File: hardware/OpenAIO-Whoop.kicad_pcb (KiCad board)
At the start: 6 copper layers, 30.3 x 30.3 mm, 266 parts, among them J1 U.FL, J10 M3, J13 M4, J16 TP0, J17 RP0, J18 5V, J19 GND, J2 +, J20 LED, J21 BZ+, J22 BZ-, J23 CAM, J24 5V, J25 GND, J26 VHD, J27 GND, J28 TX1, J29 RX1, J3 -, J31 USB, J32 CAM, J33 GND, J4 M1, J7 M2, Q26 AP1606, Q27 BC857BM, Q28 AP1606, Q29 AGM210MAP, Q30 AGM210MAP, Q31 AGM210MAP, Q32 AGM210MAP, Q33 AGM210MAP, Q34 AGM210MAP, Q35 AGM210MAP, Q36 AGM210MAP, Q37 AGM210MAP, Q38 AGM210MAP, Q39 AGM210MAP, Q40 AGM210MAP, SW1 SKUBAAE010, U1 INA186A3, U10 RP2354A, U11 BMI270, U12 TPS7A2018, U13 PY25Q128HA-DFH-IR, U14 SN74LVC1G3157, U15 TLV7031, U16 ESP32-PICO-V3, U18 SX1280, U19 RTC6705, U2 TPS61022, U20 SE5004L, U21 LP5912-3.3, U22 LP5907-2.85, U24 SGM40661, U3 TPS2116, U4 LP5912-3.3, U5 TPS22810, U6 EFM8BB51F16I, U7 EFM8BB51F16I, U8 EFM8BB51F16I, U9 EFM8BB51F16I, X1 12MHz 10pF, X3 52MHz TCXO, X4 8MHz 10pF

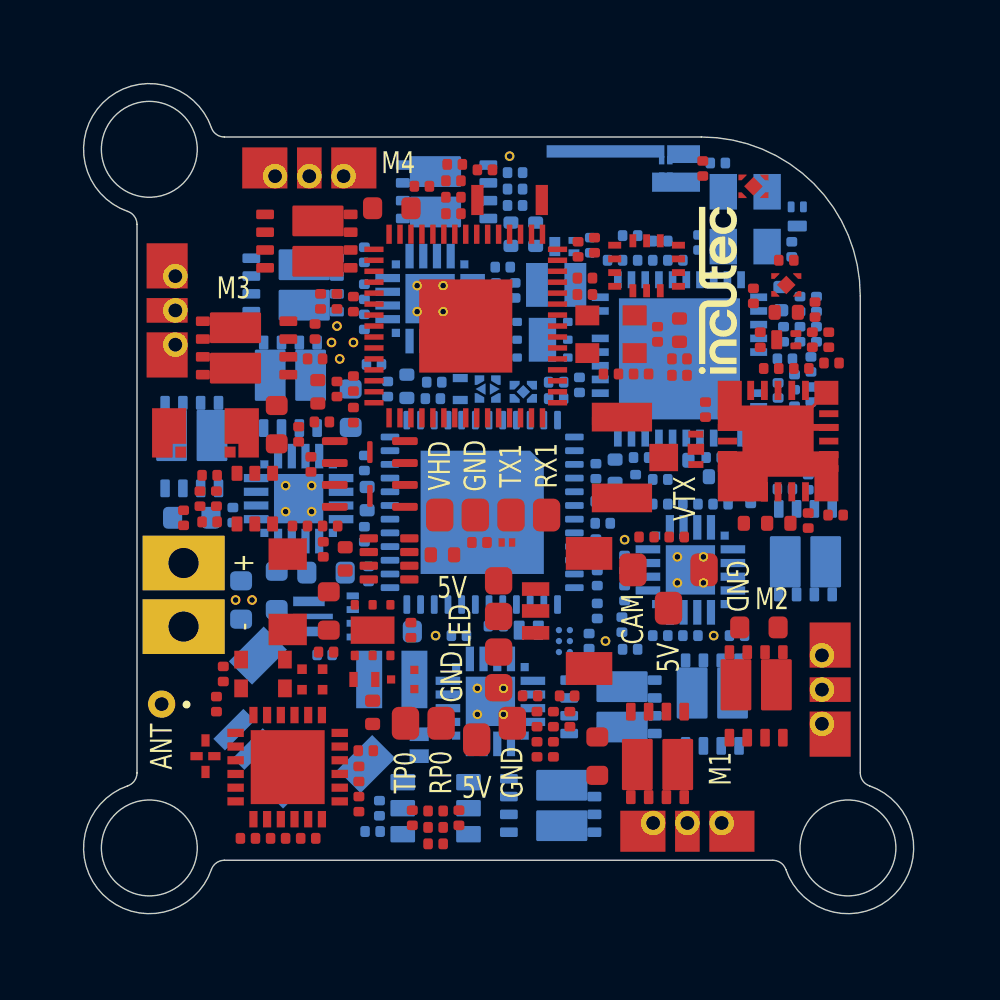
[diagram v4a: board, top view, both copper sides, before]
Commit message: hardware: floorplan v3 placed (272 footprints, Matrix-informed; DRC 0 errors, spacing 0; D72 mating zones + reserved via sites; D75 block outlines, function labels, RF paths; compaction: no empty patch > 1 mm2)
Co-Authored-By: Claude Opus 5.5 <noreply@anthropic.com>
Claude-Session: https://claude.ai/code/session_01RFaS5jnC9tnPam9GBgmGnG
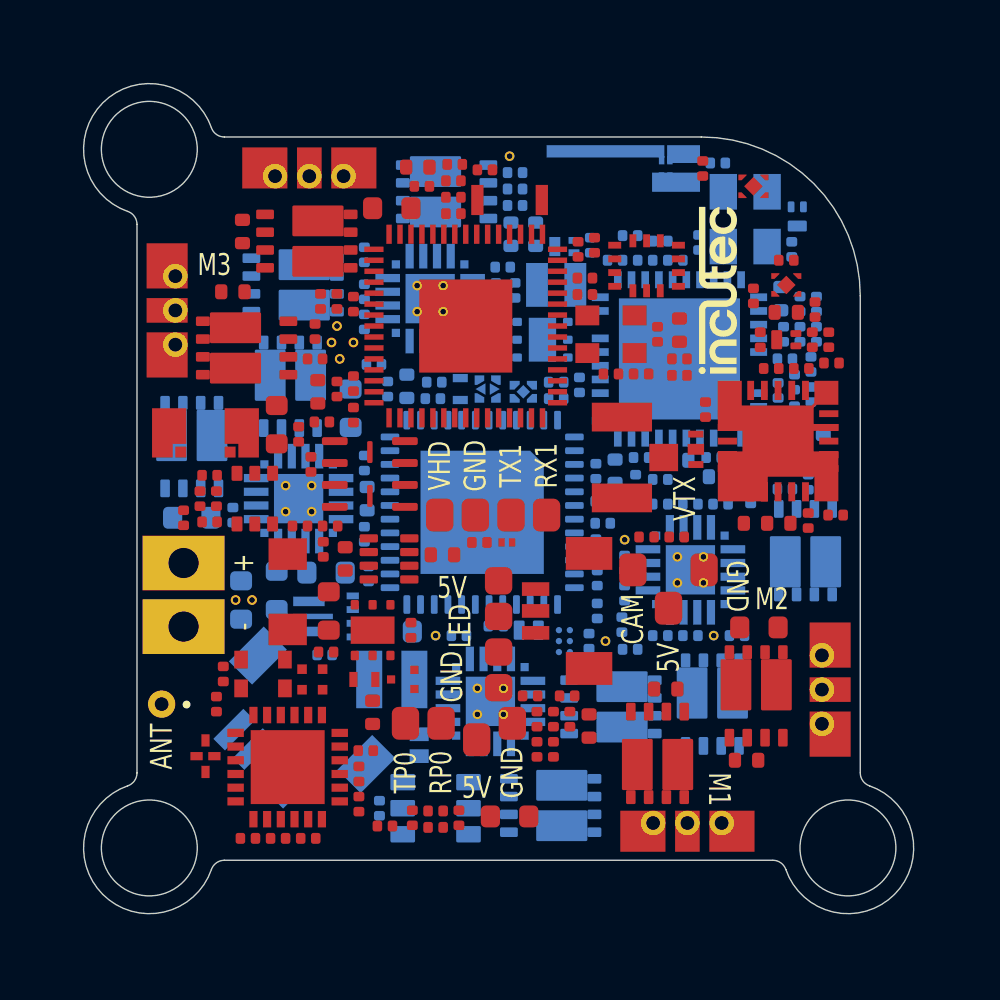
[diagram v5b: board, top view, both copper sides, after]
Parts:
- removed C17: 1uF, lib:C_0201_0603Metric_W
- removed C30: 2.2uF, lib:C_0402_1005Metric_W
- added C20: 10uF, lib:C_0402_1005Metric_W, F.Cu at (116.5, 121.5)
- added C21: 10uF, lib:C_0402_1005Metric_W, F.Cu at (119.3, 120.2)
- added C26: 10uF, lib:C_0402_1005Metric_W, B.Cu at (125.0, 111.3)
- added C27: 10uF, lib:C_0402_1005Metric_W, F.Cu at (122.2, 122.8)
- added C32: 10uF, lib:C_0402_1005Metric_W, B.Cu at (108.4, 113.2)
- added C33: 10uF, lib:C_0402_1005Metric_W, F.Cu at (103.5, 105.7)
- added C38: 10uF, lib:C_0402_1005Metric_W, F.Cu at (110.2, 101.1)
- added C39: 10uF, lib:C_0402_1005Metric_W, F.Cu at (103.8, 103.5)
- moved C23 3.88 mm to (113.6, 124.8), turned to 0 degrees
- moved R87 1.96 mm to (109.0, 125.2)
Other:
- board text removed: "M4"

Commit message: hardware: floorplan v3 review pass (RX RF corner blocker fixed; majors listed in FLOORPLAN.md Open)
Co-Authored-By: Claude Opus 5.5 <noreply@anthropic.com>
Claude-Session: https://claude.ai/code/session_01RFaS5jnC9tnPam9GBgmGnG
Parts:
- moved D4 9.68 mm to (115.3, 123.6)
- moved R7 5.25 mm to (102.9, 122.2), turned to 90 degrees
- moved C84 3.68 mm to (102.7, 123.2), turned to 0 degrees
- moved FL1 2.80 mm to (103.5, 120.0), turned to 180 degrees
- moved C85 2.32 mm to (104.6, 119.1), turned to 180 degrees
- moved X3 1.70 mm to (106.3, 119.7)

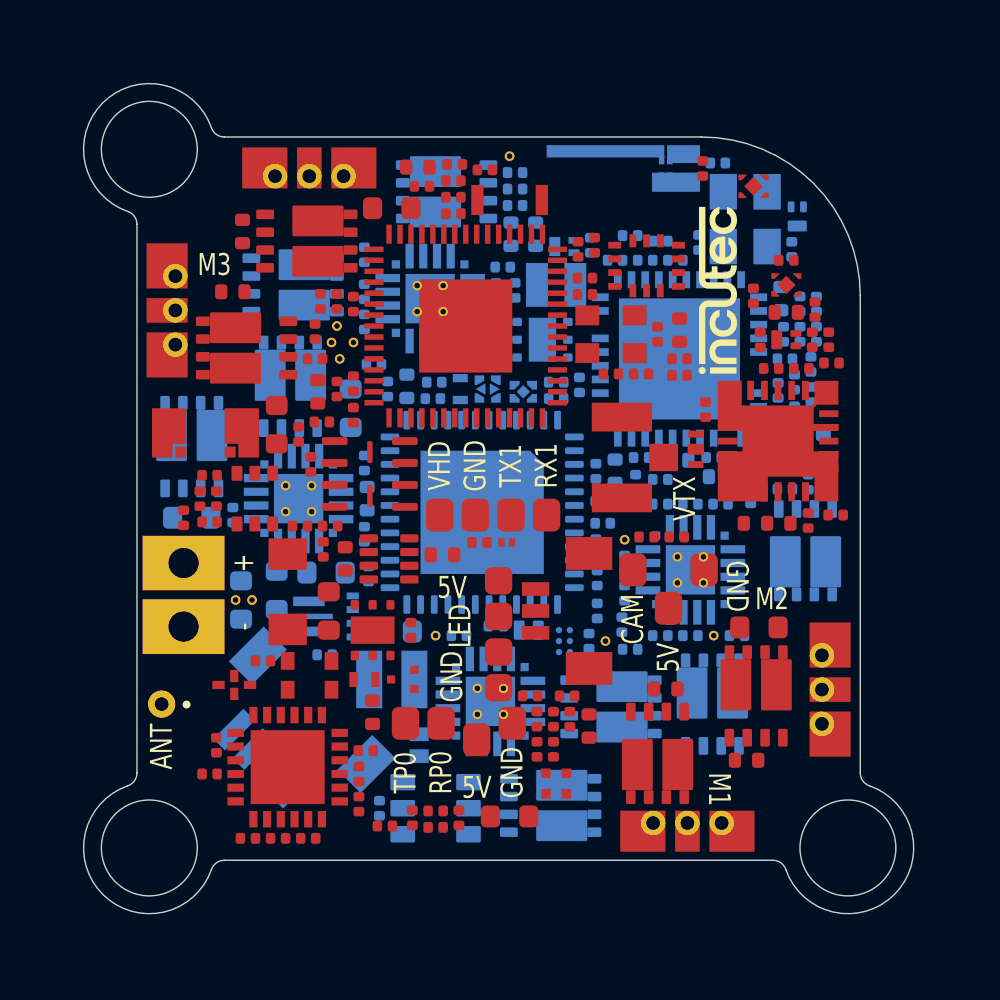
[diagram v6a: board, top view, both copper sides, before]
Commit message: hardware: schematic synced to the board (271 parts, 263 nets, parity 0 errors; SPI net patterns fixed in the DRU; X1 3225 placed)
Co-Authored-By: Claude Opus 5.5 <noreply@anthropic.com>
Claude-Session: https://claude.ai/code/session_01RFaS5jnC9tnPam9GBgmGnG
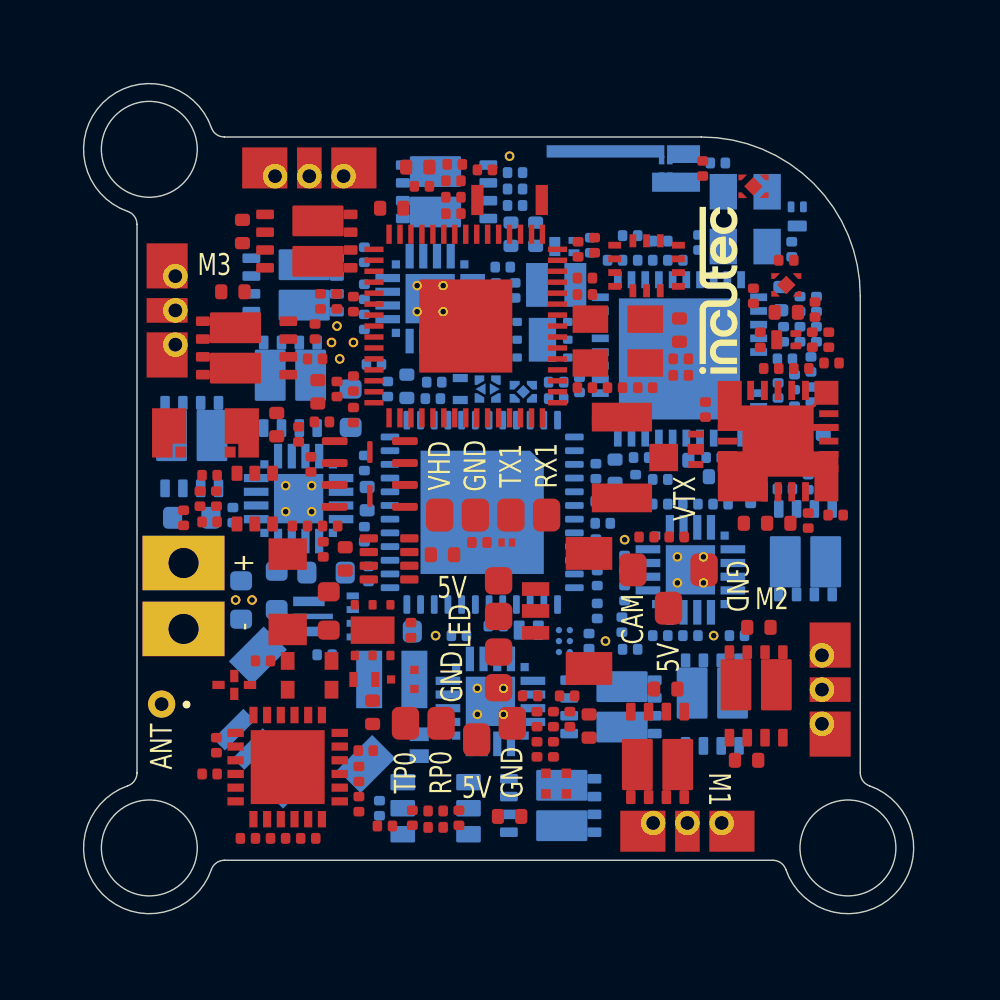
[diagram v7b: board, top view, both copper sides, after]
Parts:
- AE1: value ANT 2.4G wire -> ANT
- C124, C125: value 100nF -> 1uF
- C23, C29, C35, C41: value 22uF -> 10uF; footprint lib:C_0603_1608Metric_W -> lib:C_0402_1005Metric_W
- FL1: value LPF 2.4G -> 2450FM07D0034T; footprint lib:FILTER-SMD_4P-L1.0-W0.5-L_DEA102700LT-XXX_W -> lib:FILTER-SMD_4P-L1.0-W0.5-L_W
- J21: value BZ+ -> 5V
- R10: value 49.9k -> 18k
- R11: value 4.7k -> 2.4k
- R4: value 909k -> 47k
- R41: value 30R -> 27R
- R5: value 120k -> 6.2k
- R71, R72: value 18k -> 1k
- R73: value 10k -> 10R
- R84: value 10k -> 1k
- R9: value 80.6k -> 33k
- U18: value SX1280 -> SX1281
- X1: value 12MHz 10pF -> 12MHz; footprint lib:CRYSTAL-SMD_4P-L2.5-W2.0-BL-A_Dense -> lib:CRYSTAL-SMD_4P-L3.2-W2.5-BL_Dense
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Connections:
- AE1 pad 1: (no net) -> /RX/RF_RX_ANT
- AE2 pad 1: /FLOORPLAN/AE2_1_4 -> /RX/RF_WIFI_ANT
- AE2 pad 2: /FLOORPLAN/AE2_2 -> GND
- AE2 pad 3: /FLOORPLAN/AE2_3 -> GND
- AE2 pad 4: /FLOORPLAN/AE2_1_4 -> /RX/RF_WIFI_ANT
- C1 pad 1: (no net) -> +BATT_IN
- C1 pad 2: (no net) -> GND
- C10 pad 1: (no net) -> +5V_BST
- C10 pad 2: (no net) -> GND
- C100 pad 1: (no net) -> +3V3_VTX
- C100 pad 2: (no net) -> GND
- C101 pad 1: (no net) -> +3V3_VTX
- C101 pad 2: (no net) -> GND
- C102 pad 1: (no net) -> +3V3_VTX
- C102 pad 2: (no net) -> GND
- C103 pad 1: (no net) -> +3V3_VTX
- C103 pad 2: (no net) -> GND
- C104 pad 1: (no net) -> /VIDEO_OUT
- C104 pad 2: (no net) -> /VTX/VT_MOD_N1
- C105 pad 1: (no net) -> /VTX/VT_MOD_N1
- C105 pad 2: (no net) -> /VTX/VT_MOD_N2
- C106 pad 1: (no net) -> /VTX/RTC_VT
- C106 pad 2: (no net) -> GND
- C107 pad 1: (no net) -> /VTX/RTC_LF
- C107 pad 2: (no net) -> GND
- C108 pad 1: (no net) -> +3V3_VTX
- C108 pad 2: (no net) -> GND
- C109 pad 1: (no net) -> /VTX/PAOUT1_SUP
- C109 pad 2: (no net) -> GND
- C11 pad 1: (no net) -> +5V_BST
- C11 pad 2: (no net) -> GND
- C110 pad 1: (no net) -> /VTX/RF_PAOUT1
- C110 pad 2: (no net) -> /VTX/RF_PA_IN
- C111 pad 1: (no net) -> /VTX/PA_VCC
- C111 pad 2: (no net) -> GND
- C112 pad 1: (no net) -> /VTX/PA_VCC
- C112 pad 2: (no net) -> GND
- C113 pad 1: (no net) -> /VTX/PA_VCC
- C113 pad 2: (no net) -> GND
- C114 pad 1: (no net) -> /VTX/PA_VCC
- C114 pad 2: (no net) -> GND
- C115 pad 1: (no net) -> /VTX/PA_VCC
- C115 pad 2: (no net) -> GND
- C116 pad 1: (no net) -> /VTX/PA_VCC
- C116 pad 2: (no net) -> GND
- C117 pad 1: (no net) -> /PA_DET
- C117 pad 2: (no net) -> GND
- C118 pad 1: (no net) -> /VTX/PA_VCC
- C118 pad 2: (no net) -> GND
- C12 pad 1: (no net) -> +5V
- C12 pad 2: (no net) -> GND
- C121 pad 1: (no net) -> +3V3_VTX
- C121 pad 2: (no net) -> GND
- C122 pad 1: (no net) -> +3V3_VTX
- C122 pad 2: (no net) -> GND
- C123 pad 1: (no net) -> /VTX/PA_VREF
- C123 pad 2: (no net) -> GND
- C124 pad 1: (no net) -> /VTX/PA_RC1
- C124 pad 2: (no net) -> GND
- C125 pad 1: (no net) -> /VTX/Q27_B
- C125 pad 2: (no net) -> GND
- C128 pad 1: (no net) -> +5V_USB
- C128 pad 2: (no net) -> GND
- C129 pad 1: (no net) -> /POWER/U5_EN
- C129 pad 2: (no net) -> GND
- C13 pad 1: (no net) -> +5V
- C13 pad 2: (no net) -> GND
- C131 pad 1: (no net) -> /VBUS
- C131 pad 2: (no net) -> GND
- C132 pad 1: (no net) -> /RX/RF_WIFI_ANT
- C132 pad 2: (no net) -> GND
- C133 pad 1: (no net) -> /RX/RF_WIFI
- C133 pad 2: (no net) -> GND
- C134 pad 1: (no net) -> +1V1
- C134 pad 2: (no net) -> GND
- C14 pad 1: (no net) -> +3V3
- C14 pad 2: (no net) -> GND
- C15 pad 1: (no net) -> +5V_CAM
- C15 pad 2: (no net) -> GND
- C16 pad 1: (no net) -> /POWER/U5_CT
- C16 pad 2: (no net) -> GND
- C19 pad 1: (no net) -> +BATT
- C19 pad 2: (no net) -> GND
- C2 pad 1: (no net) -> +BATT_IN
- C2 pad 2: (no net) -> GND
- C20 pad 1: (no net) -> +BATT
- C20 pad 2: (no net) -> GND
- C21 pad 1: (no net) -> +BATT
- C21 pad 2: (no net) -> GND
- C23 pad 1: (no net) -> +BATT
- C23 pad 2: (no net) -> GND
- C25 pad 1: (no net) -> +BATT
- C25 pad 2: (no net) -> GND
- C26 pad 1: (no net) -> +BATT
- C26 pad 2: (no net) -> GND
- C27 pad 1: (no net) -> +BATT
- C27 pad 2: (no net) -> GND
- C29 pad 1: (no net) -> +BATT
- C29 pad 2: (no net) -> GND
- C31 pad 1: (no net) -> +BATT
- C31 pad 2: (no net) -> GND
- C32 pad 1: (no net) -> +BATT
- C32 pad 2: (no net) -> GND
- C33 pad 1: (no net) -> +BATT
- C33 pad 2: (no net) -> GND
- C35 pad 1: (no net) -> +BATT
- C35 pad 2: (no net) -> GND
- C37 pad 1: (no net) -> +BATT
- C37 pad 2: (no net) -> GND
- C38 pad 1: (no net) -> +BATT
- C38 pad 2: (no net) -> GND
- C39 pad 1: (no net) -> +BATT
- C39 pad 2: (no net) -> GND
- C41 pad 1: (no net) -> +BATT
- C41 pad 2: (no net) -> GND
- C42 pad 1: (no net) -> /RP2350A/XIN
- C42 pad 2: (no net) -> GND
- C43 pad 1: (no net) -> /RP2350A/XOUT_X
- C43 pad 2: (no net) -> GND
- C44 pad 1: (no net) -> +3V3
- C44 pad 2: (no net) -> GND
- C45 pad 1: (no net) -> +3V3
- C45 pad 2: (no net) -> GND
- C46 pad 1: (no net) -> +3V3
- C46 pad 2: (no net) -> GND
- C47 pad 1: (no net) -> +3V3
- C47 pad 2: (no net) -> GND
- C48 pad 1: (no net) -> +3V3
- C48 pad 2: (no net) -> GND
- C49 pad 1: (no net) -> +3V3
- C49 pad 2: (no net) -> GND
- C5 pad 1: (no net) -> /POWER/SHUNT_SENSE_N_RC
- C5 pad 2: (no net) -> /POWER/SHUNT_SENSE_P_RC
- C50 pad 1: (no net) -> +1V1
- C50 pad 2: (no net) -> GND
- C51 pad 1: (no net) -> +1V1
- C51 pad 2: (no net) -> GND
- C52 pad 1: (no net) -> +1V1
- C52 pad 2: (no net) -> GND
- C54 pad 1: (no net) -> +3V3
- C54 pad 2: (no net) -> GND
- C56 pad 1: (no net) -> +1V1
- C56 pad 2: (no net) -> GND
- C57 pad 1: (no net) -> /RP2350A/VREG_AVDD
- C57 pad 2: (no net) -> GND
- C58 pad 1: (no net) -> +3V3
- C58 pad 2: (no net) -> GND
- C59 pad 1: (no net) -> GND
- C59 pad 2: (no net) -> /RP2350A/ADC_VBAT
- C6 pad 1: (no net) -> +3V3
- C6 pad 2: (no net) -> GND
- C60 pad 1: (no net) -> /RP2350A/ADC_CURR
- C60 pad 2: (no net) -> GND
- C61 pad 1: (no net) -> +3V3
- C61 pad 2: (no net) -> GND
- C62 pad 1: (no net) -> +1V8
- C62 pad 2: (no net) -> GND
- C65 pad 1: (no net) -> +3V3
- C65 pad 2: (no net) -> GND
- C66 pad 1: (no net) -> /VIDEO_IN
- C66 pad 2: (no net) -> GND
- C67 pad 1: (no net) -> /OSD/VID_FILT
- C67 pad 2: (no net) -> GND
- C68 pad 1: (no net) -> /OSD/VID_FILT
- C68 pad 2: (no net) -> /OSD/VID_DC
- C7 pad 1: (no net) -> +BATT
- C7 pad 2: (no net) -> GND
- C70 pad 1: (no net) -> +3V3
- C70 pad 2: (no net) -> GND
- C73 pad 1: (no net) -> /RX/RX_EN
- C73 pad 2: (no net) -> GND
- C76 pad 1: (no net) -> +3V3
- C76 pad 2: (no net) -> GND
- C8 pad 1: (no net) -> +5V_BST
- C8 pad 2: (no net) -> GND
- C82 pad 1: (no net) -> +3V3
- C82 pad 2: (no net) -> GND
- C83 pad 1: (no net) -> +3V3
- C83 pad 2: (no net) -> GND
- C84 pad 1: (no net) -> /RX/TCXO_OUT
- C84 pad 2: (no net) -> /RX/XTA
- C85 pad 1: (no net) -> +3V3
- C85 pad 2: (no net) -> GND
- C86 pad 1: (no net) -> /RX/VR_PA
- C86 pad 2: (no net) -> GND
- C87 pad 1: (no net) -> GND
- C87 pad 2: (no net) -> /RX/VREG_RADIO
- C88 pad 1: (no net) -> GND
- C88 pad 2: (no net) -> /RX/VREG_RADIO
- C89 pad 1: (no net) -> +3V3
- C89 pad 2: (no net) -> GND
- C9 pad 1: (no net) -> +5V_BST
- C9 pad 2: (no net) -> GND
- C91 pad 1: (no net) -> +3V3
- C91 pad 2: (no net) -> GND
- C92 pad 1: (no net) -> +3V3
- C92 pad 2: (no net) -> GND
- C94 pad 1: (no net) -> /VTX/U19_XTAL1
- C94 pad 2: (no net) -> GND
- C95 pad 1: (no net) -> /VTX/U19_XTAL2
- C95 pad 2: (no net) -> GND
- C96 pad 1: (no net) -> /VTX/U19_REG1D8
- C96 pad 2: (no net) -> GND
- C98 pad 1: (no net) -> +3V3_VTX
- C98 pad 2: (no net) -> GND
- D1 pad 1: (no net) -> +BATT_IN
- D1 pad 2: (no net) -> GND
- D2 pad 1: (no net) -> /HD_EN
- D2 pad 2: (no net) -> /POWER/U5_EN
- D3 pad 1: (no net) -> /OSD/VID_DC
- D3 pad 2: (no net) -> GND
- D4 pad 1: (no net) -> unconnected-(D4-DOUT-Pad1)
- D4 pad 2: (no net) -> +3V3
- D4 pad 3: (no net) -> GND
- D4 pad 4: (no net) -> /RX/RX_LED
- D5 pad 1: (no net) -> /LED/D5_K
- D5 pad 2: (no net) -> +3V3
- D6 pad 1: (no net) -> /LED/D6_K
- D6 pad 2: (no net) -> +3V3
- D7 pad 1: (no net) -> /USB_D_P
- D7 pad 2: (no net) -> /USB_D_N
- D7 pad 3: (no net) -> GND
- D8 pad 1: (no net) -> /FC_BOOT
- D8 pad 2: (no net) -> /RX/RX_BOOT
- D8 pad 3: (no net) -> /RX/BOOT_SW
- FB1 pad 1: (no net) -> +5V
- FB1 pad 2: (no net) -> +5V_CAM
- FL1 pad 1: (no net) -> /RX/RF_RFIO
- FL1 pad 2: (no net) -> GND
- FL1 pad 3: (no net) -> /RX/RF_RX_ANT
- FL1 pad 4: (no net) -> GND
- FL2 pad 1: (no net) -> /VTX/RF_PA_OUT
- FL2 pad 2: (no net) -> GND
- FL2 pad 3: (no net) -> /VTX/RF_UFL
- J1 pad 1: (no net) -> /VTX/RF_UFL
- J1 pad 2: (no net) -> GND
- J1 pad 3: (no net) -> GND
- J10 pad 1: /FLOORPLAN/J10_1 -> /ESC3/PHASE_C
- J10 pad 2: /FLOORPLAN/J10_2 -> /ESC3/PHASE_B
- J10 pad 3: /FLOORPLAN/J10_3 -> /ESC3/PHASE_A
- J13 pad 1: /FLOORPLAN/J13_1 -> /ESC4/PHASE_C
- J13 pad 2: /FLOORPLAN/J13_2 -> /ESC4/PHASE_B
- J13 pad 3: /FLOORPLAN/J13_3 -> /ESC4/PHASE_A
- J16 pad 1: (no net) -> /PIOUART0_TX
- J17 pad 1: (no net) -> /PIOUART0_RX
- J18 pad 1: (no net) -> +5V
- J19 pad 1: /FLOORPLAN/GND -> GND
- J2 pad 1: (no net) -> +BATT_IN
- J20 pad 1: (no net) -> /LED_STRIP
- J21 pad 1: (no net) -> +5V
- J22 pad 1: (no net) -> /BUZZER-
- J23 pad 1: (no net) -> /VIDEO_IN
- J24 pad 1: (no net) -> +5V_CAM
- J25 pad 1: /FLOORPLAN/GND -> GND
- J26 pad 1: (no net) -> +5V_HD
- J27 pad 1: (no net) -> GND
- J28 pad 1: (no net) -> /UART1_TX
- J29 pad 1: (no net) -> /UART1_RX
- J3 pad 1: (no net) -> GND
- J31 pad 1: (no net) -> GND
- J31 pad 2: (no net) -> /USB_D_N
- J31 pad 3: (no net) -> /USB_D_P
- J31 pad 4: (no net) -> /VBUS
- J31 pad 5: (no net) -> GND
- J31 pad 6: (no net) -> GND
- J32 pad 1: (no net) -> /VIDEO_IN
- J32 pad 2: (no net) -> GND
- J32 pad 3: (no net) -> +5V_CAM
- J32 pad 4: (no net) -> GND
- J32 pad 5: (no net) -> GND
- J33 pad 1: /FLOORPLAN/GND -> GND
- J4 pad 1: /FLOORPLAN/J4_1 -> /ESC1/PHASE_C
- J4 pad 2: /FLOORPLAN/J4_2 -> /ESC1/PHASE_B
- J4 pad 3: /FLOORPLAN/J4_3 -> /ESC1/PHASE_A
- J7 pad 1: /FLOORPLAN/J7_1 -> /ESC2/PHASE_C
- J7 pad 2: /FLOORPLAN/J7_2 -> /ESC2/PHASE_B
- J7 pad 3: /FLOORPLAN/J7_3 -> /ESC2/PHASE_A
- L1 pad 1: (no net) -> +BATT
- L1 pad 2: (no net) -> /POWER/U2_SW
- L2 pad 1: (no net) -> +1V1
- L2 pad 2: (no net) -> /RP2350A/VREG_LX
- L3 pad 1: (no net) -> /VTX/PAOUT1_SUP
- L3 pad 2: (no net) -> /VTX/RF_PAOUT1
- Q26 pad 1: (no net) -> /RP2350A/BEEPER
- Q26 pad 2: (no net) -> GND
- Q26 pad 3: (no net) -> /BUZZER-
- Q27 pad 1: (no net) -> /VTX/Q27_B
- Q27 pad 2: (no net) -> /VTX/Q27_E
- Q27 pad 3: (no net) -> /VTX/Q27_C
- Q28 pad 1: (no net) -> /HD_EN
- Q28 pad 2: (no net) -> GND
- Q28 pad 3: (no net) -> /VTX/VTX_PWR_EN
- Q29 pad 1: (no net) -> GND
- Q29 pad 2: (no net) -> /ESC1/A_PWM
- Q29 pad 3: (no net) -> +BATT
- Q29 pad 4: (no net) -> /ESC1/A_COM
- Q29 pad 5: /FLOORPLAN/Q29_5_6_7_8 -> /ESC1/PHASE_A
- Q29 pad 6: /FLOORPLAN/Q29_5_6_7_8 -> /ESC1/PHASE_A
- Q29 pad 7: /FLOORPLAN/Q29_5_6_7_8 -> /ESC1/PHASE_A
- Q29 pad 8: /FLOORPLAN/Q29_5_6_7_8 -> /ESC1/PHASE_A
- Q30 pad 1: (no net) -> GND
- Q30 pad 2: (no net) -> /ESC1/B_PWM
- Q30 pad 3: (no net) -> +BATT
- Q30 pad 4: (no net) -> /ESC1/B_COM
- Q30 pad 5: /FLOORPLAN/Q30_5_6_7_8 -> /ESC1/PHASE_B
- Q30 pad 6: /FLOORPLAN/Q30_5_6_7_8 -> /ESC1/PHASE_B
- Q30 pad 7: /FLOORPLAN/Q30_5_6_7_8 -> /ESC1/PHASE_B
- Q30 pad 8: /FLOORPLAN/Q30_5_6_7_8 -> /ESC1/PHASE_B
- Q31 pad 1: (no net) -> GND
- Q31 pad 2: (no net) -> /ESC1/C_PWM
- Q31 pad 3: (no net) -> +BATT
- Q31 pad 4: (no net) -> /ESC1/C_COM
- Q31 pad 5: /FLOORPLAN/Q31_5_6_7_8 -> /ESC1/PHASE_C
- Q31 pad 6: /FLOORPLAN/Q31_5_6_7_8 -> /ESC1/PHASE_C
- Q31 pad 7: /FLOORPLAN/Q31_5_6_7_8 -> /ESC1/PHASE_C
- Q31 pad 8: /FLOORPLAN/Q31_5_6_7_8 -> /ESC1/PHASE_C
- Q32 pad 1: (no net) -> GND
- Q32 pad 2: (no net) -> /ESC2/A_PWM
- Q32 pad 3: (no net) -> +BATT
- Q32 pad 4: (no net) -> /ESC2/A_COM
- Q32 pad 5: /FLOORPLAN/Q32_5_6_7_8 -> /ESC2/PHASE_A
- Q32 pad 6: /FLOORPLAN/Q32_5_6_7_8 -> /ESC2/PHASE_A
- Q32 pad 7: /FLOORPLAN/Q32_5_6_7_8 -> /ESC2/PHASE_A
- Q32 pad 8: /FLOORPLAN/Q32_5_6_7_8 -> /ESC2/PHASE_A
- Q33 pad 1: (no net) -> GND
- Q33 pad 2: (no net) -> /ESC2/B_PWM
- Q33 pad 3: (no net) -> +BATT
- Q33 pad 4: (no net) -> /ESC2/B_COM
- Q33 pad 5: /FLOORPLAN/Q33_5_6_7_8 -> /ESC2/PHASE_B
- Q33 pad 6: /FLOORPLAN/Q33_5_6_7_8 -> /ESC2/PHASE_B
- Q33 pad 7: /FLOORPLAN/Q33_5_6_7_8 -> /ESC2/PHASE_B
- Q33 pad 8: /FLOORPLAN/Q33_5_6_7_8 -> /ESC2/PHASE_B
- Q34 pad 1: (no net) -> GND
- Q34 pad 2: (no net) -> /ESC2/C_PWM
- Q34 pad 3: (no net) -> +BATT
- Q34 pad 4: (no net) -> /ESC2/C_COM
- Q34 pad 5: /FLOORPLAN/Q34_5_6_7_8 -> /ESC2/PHASE_C
- Q34 pad 6: /FLOORPLAN/Q34_5_6_7_8 -> /ESC2/PHASE_C
- Q34 pad 7: /FLOORPLAN/Q34_5_6_7_8 -> /ESC2/PHASE_C
- Q34 pad 8: /FLOORPLAN/Q34_5_6_7_8 -> /ESC2/PHASE_C
- Q35 pad 1: (no net) -> GND
- Q35 pad 2: (no net) -> /ESC3/A_PWM
- Q35 pad 3: (no net) -> +BATT
- Q35 pad 4: (no net) -> /ESC3/A_COM
- Q35 pad 5: /FLOORPLAN/Q35_5_6_7_8 -> /ESC3/PHASE_A
- Q35 pad 6: /FLOORPLAN/Q35_5_6_7_8 -> /ESC3/PHASE_A
- Q35 pad 7: /FLOORPLAN/Q35_5_6_7_8 -> /ESC3/PHASE_A
- Q35 pad 8: /FLOORPLAN/Q35_5_6_7_8 -> /ESC3/PHASE_A
- Q36 pad 1: (no net) -> GND
- Q36 pad 2: (no net) -> /ESC3/B_PWM
- Q36 pad 3: (no net) -> +BATT
- Q36 pad 4: (no net) -> /ESC3/B_COM
- Q36 pad 5: /FLOORPLAN/Q36_5_6_7_8 -> /ESC3/PHASE_B
- Q36 pad 6: /FLOORPLAN/Q36_5_6_7_8 -> /ESC3/PHASE_B
- Q36 pad 7: /FLOORPLAN/Q36_5_6_7_8 -> /ESC3/PHASE_B
- Q36 pad 8: /FLOORPLAN/Q36_5_6_7_8 -> /ESC3/PHASE_B
- Q37 pad 1: (no net) -> GND
- Q37 pad 2: (no net) -> /ESC3/C_PWM
- Q37 pad 3: (no net) -> +BATT
- Q37 pad 4: (no net) -> /ESC3/C_COM
- Q37 pad 5: /FLOORPLAN/Q37_5_6_7_8 -> /ESC3/PHASE_C
- Q37 pad 6: /FLOORPLAN/Q37_5_6_7_8 -> /ESC3/PHASE_C
- Q37 pad 7: /FLOORPLAN/Q37_5_6_7_8 -> /ESC3/PHASE_C
- Q37 pad 8: /FLOORPLAN/Q37_5_6_7_8 -> /ESC3/PHASE_C
- Q38 pad 1: (no net) -> GND
- Q38 pad 2: (no net) -> /ESC4/A_PWM
- Q38 pad 3: (no net) -> +BATT
- Q38 pad 4: (no net) -> /ESC4/A_COM
- Q38 pad 5: /FLOORPLAN/Q38_5_6_7_8 -> /ESC4/PHASE_A
- Q38 pad 6: /FLOORPLAN/Q38_5_6_7_8 -> /ESC4/PHASE_A
- Q38 pad 7: /FLOORPLAN/Q38_5_6_7_8 -> /ESC4/PHASE_A
- Q38 pad 8: /FLOORPLAN/Q38_5_6_7_8 -> /ESC4/PHASE_A
- Q39 pad 1: (no net) -> GND
- Q39 pad 2: (no net) -> /ESC4/B_PWM
- Q39 pad 3: (no net) -> +BATT
- Q39 pad 4: (no net) -> /ESC4/B_COM
- Q39 pad 5: /FLOORPLAN/Q39_5_6_7_8 -> /ESC4/PHASE_B
- Q39 pad 6: /FLOORPLAN/Q39_5_6_7_8 -> /ESC4/PHASE_B
- Q39 pad 7: /FLOORPLAN/Q39_5_6_7_8 -> /ESC4/PHASE_B
- Q39 pad 8: /FLOORPLAN/Q39_5_6_7_8 -> /ESC4/PHASE_B
- Q40 pad 1: (no net) -> GND
- Q40 pad 2: (no net) -> /ESC4/C_PWM
- Q40 pad 3: (no net) -> +BATT
- Q40 pad 4: (no net) -> /ESC4/C_COM
- Q40 pad 5: /FLOORPLAN/Q40_5_6_7_8 -> /ESC4/PHASE_C
- Q40 pad 6: /FLOORPLAN/Q40_5_6_7_8 -> /ESC4/PHASE_C
- Q40 pad 7: /FLOORPLAN/Q40_5_6_7_8 -> /ESC4/PHASE_C
- Q40 pad 8: /FLOORPLAN/Q40_5_6_7_8 -> /ESC4/PHASE_C
- R1 pad 1: (no net) -> +BATT_IN
- R1 pad 2: (no net) -> /POWER/SHUNT_SENSE_P
- R1 pad 3: (no net) -> /POWER/SHUNT_SENSE_N
- R1 pad 4: (no net) -> +BATT
- R10 pad 1: (no net) -> /POWER/U5_EN
- R10 pad 2: (no net) -> GND
- R11 pad 1: (no net) -> /HD_EN
- R11 pad 2: (no net) -> GND
- R12 pad 1: (no net) -> /MOTOR1
- R12 pad 2: (no net) -> /ESC1/RTX
- R13 pad 1: (no net) -> /ESC1/PHASE_A
- R13 pad 2: (no net) -> /ESC1/BEMF_A
- R14 pad 1: (no net) -> /ESC1/PHASE_B
- R14 pad 2: (no net) -> /ESC1/BEMF_B
- R15 pad 1: (no net) -> /ESC1/PHASE_C
- R15 pad 2: (no net) -> /ESC1/BEMF_C
- R16 pad 1: (no net) -> /ESC1/PHASE_A
- R16 pad 2: (no net) -> /ESC1/NEUTRAL
- R17 pad 1: (no net) -> /ESC1/PHASE_B
- R17 pad 2: (no net) -> /ESC1/NEUTRAL
- R18 pad 1: (no net) -> /ESC1/PHASE_C
- R18 pad 2: (no net) -> /ESC1/NEUTRAL
- R19 pad 1: (no net) -> /MOTOR2
- R19 pad 2: (no net) -> /ESC2/RTX
- R2 pad 1: (no net) -> /POWER/SHUNT_SENSE_P
- R2 pad 2: (no net) -> /POWER/SHUNT_SENSE_P_RC
- R20 pad 1: (no net) -> /ESC2/PHASE_A
- R20 pad 2: (no net) -> /ESC2/BEMF_A
- R21 pad 1: (no net) -> /ESC2/PHASE_B
- R21 pad 2: (no net) -> /ESC2/BEMF_B
- R22 pad 1: (no net) -> /ESC2/PHASE_C
- R22 pad 2: (no net) -> /ESC2/BEMF_C
- R23 pad 1: (no net) -> /ESC2/PHASE_A
- R23 pad 2: (no net) -> /ESC2/NEUTRAL
- R24 pad 1: (no net) -> /ESC2/PHASE_B
- R24 pad 2: (no net) -> /ESC2/NEUTRAL
- R25 pad 1: (no net) -> /ESC2/PHASE_C
- R25 pad 2: (no net) -> /ESC2/NEUTRAL
- R26 pad 1: (no net) -> /MOTOR3
- R26 pad 2: (no net) -> /ESC3/RTX
- R27 pad 1: (no net) -> /ESC3/PHASE_A
- R27 pad 2: (no net) -> /ESC3/BEMF_A
- R28 pad 1: (no net) -> /ESC3/PHASE_B
- R28 pad 2: (no net) -> /ESC3/BEMF_B
- R29 pad 1: (no net) -> /ESC3/PHASE_C
- R29 pad 2: (no net) -> /ESC3/BEMF_C
- R3 pad 1: (no net) -> /POWER/SHUNT_SENSE_N
- R3 pad 2: (no net) -> /POWER/SHUNT_SENSE_N_RC
- R30 pad 1: (no net) -> /ESC3/PHASE_A
- R30 pad 2: (no net) -> /ESC3/NEUTRAL
- R31 pad 1: (no net) -> /ESC3/PHASE_B
- R31 pad 2: (no net) -> /ESC3/NEUTRAL
- R32 pad 1: (no net) -> /ESC3/PHASE_C
- R32 pad 2: (no net) -> /ESC3/NEUTRAL
- R33 pad 1: (no net) -> /MOTOR4
- R33 pad 2: (no net) -> /ESC4/RTX
- R34 pad 1: (no net) -> /ESC4/PHASE_A
- R34 pad 2: (no net) -> /ESC4/BEMF_A
- R35 pad 1: (no net) -> /ESC4/PHASE_B
- R35 pad 2: (no net) -> /ESC4/BEMF_B
- R36 pad 1: (no net) -> /ESC4/PHASE_C
- R36 pad 2: (no net) -> /ESC4/BEMF_C
- R37 pad 1: (no net) -> /ESC4/PHASE_A
- R37 pad 2: (no net) -> /ESC4/NEUTRAL
- R38 pad 1: (no net) -> /ESC4/PHASE_B
- R38 pad 2: (no net) -> /ESC4/NEUTRAL
- R39 pad 1: (no net) -> /ESC4/PHASE_C
- R39 pad 2: (no net) -> /ESC4/NEUTRAL
- R4 pad 1: (no net) -> +5V_BST
- R4 pad 2: (no net) -> /POWER/U2_FB
- R40 pad 1: (no net) -> /RP2350A/XOUT_X
- R40 pad 2: (no net) -> /RP2350A/XOUT
- R41 pad 1: (no net) -> +3V3
- R41 pad 2: (no net) -> /RP2350A/VREG_AVDD
- R42 pad 1: (no net) -> /RP2350A/U10_USB_DP
- R42 pad 2: (no net) -> /USB_D_P
- R43 pad 1: (no net) -> /USB_D_N
- R43 pad 2: (no net) -> /RP2350A/U10_USB_DM
- R44 pad 1: (no net) -> /RP2350A/QSPI_SS
- R44 pad 2: (no net) -> /FC_BOOT
- R45 pad 1: (no net) -> /RP2350A/ADC_VBAT
- R45 pad 2: (no net) -> +BATT
- R46 pad 1: (no net) -> GND
- R46 pad 2: (no net) -> /RP2350A/ADC_VBAT
- R47 pad 1: (no net) -> /CURR_SENSE
- R47 pad 2: (no net) -> /RP2350A/ADC_CURR
- R48 pad 1: (no net) -> GND
- R48 pad 2: (no net) -> /RP2350A/BEEPER
- R49 pad 1: (no net) -> /GYRO_CS
- R49 pad 2: (no net) -> +3V3
- R5 pad 1: (no net) -> /POWER/U2_FB
- R5 pad 2: (no net) -> GND
- R50 pad 1: (no net) -> +3V3
- R50 pad 2: (no net) -> /FLASH_CS
- R51 pad 1: (no net) -> /VIDEO_IN
- R51 pad 2: (no net) -> GND
- R52 pad 1: (no net) -> /OSD_W
- R52 pad 2: (no net) -> /OSD/OSD_LVL
- R53 pad 1: (no net) -> /OSD/OSD_LVL
- R53 pad 2: (no net) -> +3V3
- R54 pad 1: (no net) -> GND
- R54 pad 2: (no net) -> /OSD/OSD_LVL
- R55 pad 1: (no net) -> /OSD/VID_FILT
- R55 pad 2: (no net) -> /VIDEO_IN
- R56 pad 1: (no net) -> +3V3
- R56 pad 2: (no net) -> /RX/RX_EN
- R58 pad 1: (no net) -> /VIDEO_OUT
- R58 pad 2: (no net) -> /VTX/VT_MOD_N1
- R59 pad 1: (no net) -> /VTX/VT_MOD_N1
- R59 pad 2: (no net) -> GND
- R60 pad 1: (no net) -> /VTX/VT_MOD_N2
- R60 pad 2: (no net) -> /VTX/VT_MOD
- R61 pad 1: (no net) -> +3V3_VTX
- R61 pad 2: (no net) -> /VTX/VT_MOD
- R62 pad 1: (no net) -> /VTX/VT_MOD
- R62 pad 2: (no net) -> GND
- R63 pad 1: (no net) -> /VTX/RTC_CP
- R63 pad 2: (no net) -> /VTX/RTC_VT
- R64 pad 1: (no net) -> /VTX/RTC_VT
- R64 pad 2: (no net) -> /VTX/RTC_LF
- R65 pad 1: (no net) -> /VTX/Q27_C
- R65 pad 2: (no net) -> /VTX/PAOUT1_SUP
- R66 pad 1: (no net) -> /VTX/PA_DET_RAW
- R66 pad 2: (no net) -> /PA_DET
- R67 pad 1: (no net) -> +BATT
- R67 pad 2: (no net) -> /VTX/PA_VCC
- R67 pad 3: (no net) -> +5V
- R68 pad 1: (no net) -> +3V3
- R68 pad 2: (no net) -> /VTX/VTX_PWR_EN
- R7 pad 1: (no net) -> +5V_USB
- R7 pad 2: (no net) -> /POWER/U3_PR1
- R70 pad 1: (no net) -> +3V3
- R70 pad 2: (no net) -> /PA_NTC
- R71 pad 1: (no net) -> /VTX_AMP_PWM
- R71 pad 2: (no net) -> /VTX/PA_RC1
- R72 pad 1: (no net) -> /VTX/PA_RC1
- R72 pad 2: (no net) -> /VTX/Q27_B
- R73 pad 1: (no net) -> +3V3_VTX
- R73 pad 2: (no net) -> /VTX/Q27_E
- R8 pad 1: (no net) -> /POWER/U3_PR1
- R8 pad 2: (no net) -> GND
- R80 pad 1: (no net) -> /VTX_SPI_CS
- R80 pad 2: (no net) -> /VTX/U19_SPILE
- R81 pad 1: (no net) -> /VTX_SPI_CLK
- R81 pad 2: (no net) -> /VTX/U19_SPICLK
- R82 pad 1: (no net) -> /VTX_SPI_DATA
- R82 pad 2: (no net) -> /VTX/U19_SPIDATA
- R84 pad 1: (no net) -> /VTX_PWR_CTL
- R84 pad 2: (no net) -> /VTX/VTX_PWR_EN
- R85 pad 1: (no net) -> /LED/D5_K
- R85 pad 2: (no net) -> /LED0
- R86 pad 1: (no net) -> /LED/D6_K
- R86 pad 2: (no net) -> /LED1
- R87 pad 1: (no net) -> +5V_HD
- R87 pad 2: (no net) -> /POWER/U5_EN
- R88 pad 1: (no net) -> /RX/RF_WIFI_ANT
- R88 pad 2: (no net) -> /RX/RF_WIFI
- R9 pad 1: (no net) -> +BATT
- R9 pad 2: (no net) -> /POWER/U5_EN
- SW1 pad 1: (no net) -> /RX/BOOT_SW
- SW1 pad 2: (no net) -> GND
- TH1 pad 1: (no net) -> /PA_NTC
- TH1 pad 2: (no net) -> GND
- TP1 pad 1: /FLOORPLAN/TP1_1 -> /ESC1/C2D
- TP12 pad 1: /FLOORPLAN/TP12_1 -> /RP2350A/SWCLK
- TP13 pad 1: /FLOORPLAN/TP13_1 -> /RP2350A/SWDIO
- TP2 pad 1: /FLOORPLAN/TP2_1 -> /ESC1/C2CK
- TP3 pad 1: /FLOORPLAN/TP3_1 -> /ESC2/C2D
- TP4 pad 1: /FLOORPLAN/TP4_1 -> /ESC2/C2CK
- TP5 pad 1: /FLOORPLAN/TP5_1 -> /ESC3/C2D
- TP6 pad 1: /FLOORPLAN/TP6_1 -> /ESC3/C2CK
- TP7 pad 1: /FLOORPLAN/TP7_1 -> /ESC4/C2D
- TP8 pad 1: /FLOORPLAN/TP8_1 -> /ESC4/C2CK
- TP9 pad 1: /FLOORPLAN/TP9_1 -> /FC_BOOT
- U1 pad 1: (no net) -> GND
- U1 pad 2: (no net) -> GND
- U1 pad 3: (no net) -> +3V3
- U1 pad 4: (no net) -> /POWER/SHUNT_SENSE_P_RC
- U1 pad 5: (no net) -> /POWER/SHUNT_SENSE_N_RC
- U1 pad 6: (no net) -> /CURR_SENSE
- U10 pad 1: (no net) -> +3V3
- U10 pad 10: (no net) -> /LED0
- U10 pad 11: (no net) -> +3V3
- U10 pad 12: (no net) -> /LED_STRIP
- U10 pad 13: (no net) -> /GYRO_INT
- U10 pad 14: (no net) -> /SPI1_SCK
- U10 pad 15: (no net) -> /SPI1_MOSI
- U10 pad 16: (no net) -> /SPI1_MISO
- U10 pad 17: (no net) -> /GYRO_CS
- U10 pad 18: (no net) -> /OSD_W
- U10 pad 19: (no net) -> /OSD_EN
- U10 pad 2: (no net) -> /UART0_TX
- U10 pad 20: (no net) -> +3V3
- U10 pad 21: (no net) -> /RP2350A/XIN
- U10 pad 22: (no net) -> /RP2350A/XOUT
- U10 pad 23: (no net) -> +1V1
- U10 pad 24: (no net) -> /RP2350A/SWCLK
- U10 pad 25: (no net) -> /RP2350A/SWDIO
- U10 pad 26: (no net) -> +3V3
- U10 pad 27: (no net) -> /OSD_SYNC
- U10 pad 28: (no net) -> /RP2350A/BEEPER
- U10 pad 29: (no net) -> /SPI0_SCK
- U10 pad 3: (no net) -> /UART0_RX
- U10 pad 30: (no net) -> +3V3
- U10 pad 31: (no net) -> /SPI0_MOSI
- U10 pad 32: (no net) -> /SPI0_MISO
- U10 pad 33: (no net) -> /FLASH_CS
- U10 pad 34: (no net) -> /MOTOR4
- U10 pad 35: (no net) -> /MOTOR3
- U10 pad 36: (no net) -> /MOTOR2
- U10 pad 37: (no net) -> /MOTOR1
- U10 pad 38: (no net) -> +3V3
- U10 pad 39: (no net) -> +1V1
- U10 pad 4: (no net) -> /PIOUART0_TX
- U10 pad 40: (no net) -> /LED1
- U10 pad 41: (no net) -> /HD_EN
- U10 pad 42: (no net) -> /RP2350A/ADC_CURR
- U10 pad 43: (no net) -> /RP2350A/ADC_VBAT
- U10 pad 44: (no net) -> +3V3
- U10 pad 45: (no net) -> +3V3
- U10 pad 46: (no net) -> /RP2350A/VREG_AVDD
- U10 pad 47: (no net) -> GND
- U10 pad 48: (no net) -> /RP2350A/VREG_LX
- U10 pad 49: (no net) -> +3V3
- U10 pad 5: (no net) -> /PIOUART0_RX
- U10 pad 50: (no net) -> +1V1
- U10 pad 51: (no net) -> /RP2350A/U10_USB_DM
- U10 pad 52: (no net) -> /RP2350A/U10_USB_DP
- U10 pad 53: (no net) -> +3V3
- U10 pad 54: (no net) -> +3V3
- U10 pad 55: (no net) -> unconnected-(U10-QSPI_SD3-Pad55)
- U10 pad 56: (no net) -> unconnected-(U10-QSPI_SCLK-Pad56)
- U10 pad 57: (no net) -> unconnected-(U10-QSPI_SD0-Pad57)
- U10 pad 58: (no net) -> unconnected-(U10-QSPI_SD2-Pad58)
- U10 pad 59: (no net) -> unconnected-(U10-QSPI_SD1-Pad59)
- U10 pad 6: (no net) -> +1V1
- U10 pad 60: (no net) -> /RP2350A/QSPI_SS
- U10 pad 61: /FLOORPLAN/GND -> GND
- U10 pad 7: (no net) -> /UART1_TX
- U10 pad 8: (no net) -> /UART1_RX
- U10 pad 9: (no net) -> /GYRO_CLKIN
- U11 pad 1: (no net) -> /SPI1_MISO
- U11 pad 10: (no net) -> unconnected-(U11-OCSB-Pad10)
- U11 pad 11: (no net) -> unconnected-(U11-OSDO-Pad11)
- U11 pad 12: (no net) -> /GYRO_CS
- U11 pad 13: (no net) -> /SPI1_SCK
- U11 pad 14: (no net) -> /SPI1_MOSI
- U11 pad 2: (no net) -> unconnected-(U11-ASDx-Pad2)
- U11 pad 3: (no net) -> unconnected-(U11-ASCx-Pad3)
- U11 pad 4: (no net) -> /GYRO_INT
- U11 pad 5: (no net) -> +3V3
- U11 pad 6: (no net) -> GND
- U11 pad 7: (no net) -> GND
- U11 pad 8: (no net) -> +1V8
- U11 pad 9: (no net) -> /GYRO_CLKIN
- U12 pad 1: (no net) -> +1V8
- U12 pad 2: (no net) -> GND
- U12 pad 3: (no net) -> +3V3
- U12 pad 4: (no net) -> +3V3
- U12 pad 5: (no net) -> GND
- U13 pad 1: (no net) -> /FLASH_CS
- U13 pad 2: (no net) -> /SPI0_MISO
- U13 pad 3: (no net) -> +3V3
- U13 pad 4: (no net) -> GND
- U13 pad 5: (no net) -> /SPI0_MOSI
- U13 pad 6: (no net) -> /SPI0_SCK
- U13 pad 7: (no net) -> +3V3
- U13 pad 8: (no net) -> +3V3
- U13 pad 9: (no net) -> unconnected-(U13-EP-Pad9)
- U14 pad 1: (no net) -> /OSD/OSD_LVL
- U14 pad 2: (no net) -> GND
- U14 pad 3: (no net) -> /VIDEO_IN
- U14 pad 4: (no net) -> /VIDEO_OUT
- U14 pad 5: (no net) -> +3V3
- U14 pad 6: (no net) -> /OSD_EN
- U15 pad 1: (no net) -> /OSD_SYNC
- U15 pad 2: (no net) -> +3V3
- U15 pad 3: (no net) -> GND
- U15 pad 4: (no net) -> GND
- U15 pad 5: (no net) -> /OSD/VID_DC
- U16 pad 1: (no net) -> +3V3
- U16 pad 10: (no net) -> /PA_NTC
- U16 pad 11: (no net) -> unconnected-(U16-VDET_2/I35-Pad11)
- U16 pad 12: (no net) -> /RX/RADIO_MOSI
- U16 pad 13: (no net) -> /RX/RADIO_MISO
- U16 pad 14: (no net) -> /RX/RADIO_SCK
- U16 pad 15: (no net) -> /RX/RADIO_RST
- U16 pad 16: (no net) -> /RX/RADIO_NSS
- U16 pad 17: (no net) -> /VTX_SPI_DATA
- U16 pad 18: (no net) -> unconnected-(U16-MTDI/IO12-Pad18)
- U16 pad 19: (no net) -> +3V3
- U16 pad 2: (no net) -> /RX/RF_WIFI
- U16 pad 20: (no net) -> /VTX_AMP_PWM
- U16 pad 21: (no net) -> unconnected-(U16-MTDO/IO15-Pad21)
- U16 pad 22: (no net) -> /PA_EN
- U16 pad 23: (no net) -> /RX/RX_BOOT
- U16 pad 24: (no net) -> /PA_DET
- U16 pad 25: (no net) -> unconnected-(U16-NC-Pad25)
- U16 pad 26: (no net) -> unconnected-(U16-VDD_SDIO-Pad26)
- U16 pad 27: (no net) -> unconnected-(U16-IO20-Pad27)
- U16 pad 28: (no net) -> unconnected-(U16-SD2/IO9-Pad28)
- U16 pad 29: (no net) -> unconnected-(U16-SD3/IO10-Pad29)
- U16 pad 3: (no net) -> +3V3
- U16 pad 30: (no net) -> unconnected-(U16-CMD/IO11_FLASH-Pad30)
- U16 pad 31: (no net) -> unconnected-(U16-CLK/IO6_FLASH-Pad31)
- U16 pad 32: (no net) -> unconnected-(U16-SD0/IO7-Pad32)
- U16 pad 33: (no net) -> unconnected-(U16-SD1/IO8-Pad33)
- U16 pad 34: (no net) -> /VTX_SPI_CLK
- U16 pad 35: (no net) -> unconnected-(U16-NC-Pad35)
- U16 pad 36: (no net) -> unconnected-(U16-NC-Pad36)
- U16 pad 37: (no net) -> +3V3
- U16 pad 38: (no net) -> /VTX_SPI_CS
- U16 pad 39: (no net) -> /RX/RX_LED
- U16 pad 4: (no net) -> +3V3
- U16 pad 40: (no net) -> /UART0_TX
- U16 pad 41: (no net) -> /UART0_RX
- U16 pad 42: (no net) -> /VTX_PWR_CTL
- U16 pad 43: (no net) -> +3V3
- U16 pad 44: (no net) -> unconnected-(U16-NC-Pad44)
- U16 pad 45: (no net) -> unconnected-(U16-NC-Pad45)
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
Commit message: wip: routing prep (zones and via fields) and schematic review round 4
Co-Authored-By: Claude Opus 5.5 <noreply@anthropic.com>
Claude-Session: https://claude.ai/code/session_01RFaS5jnC9tnPam9GBgmGnG
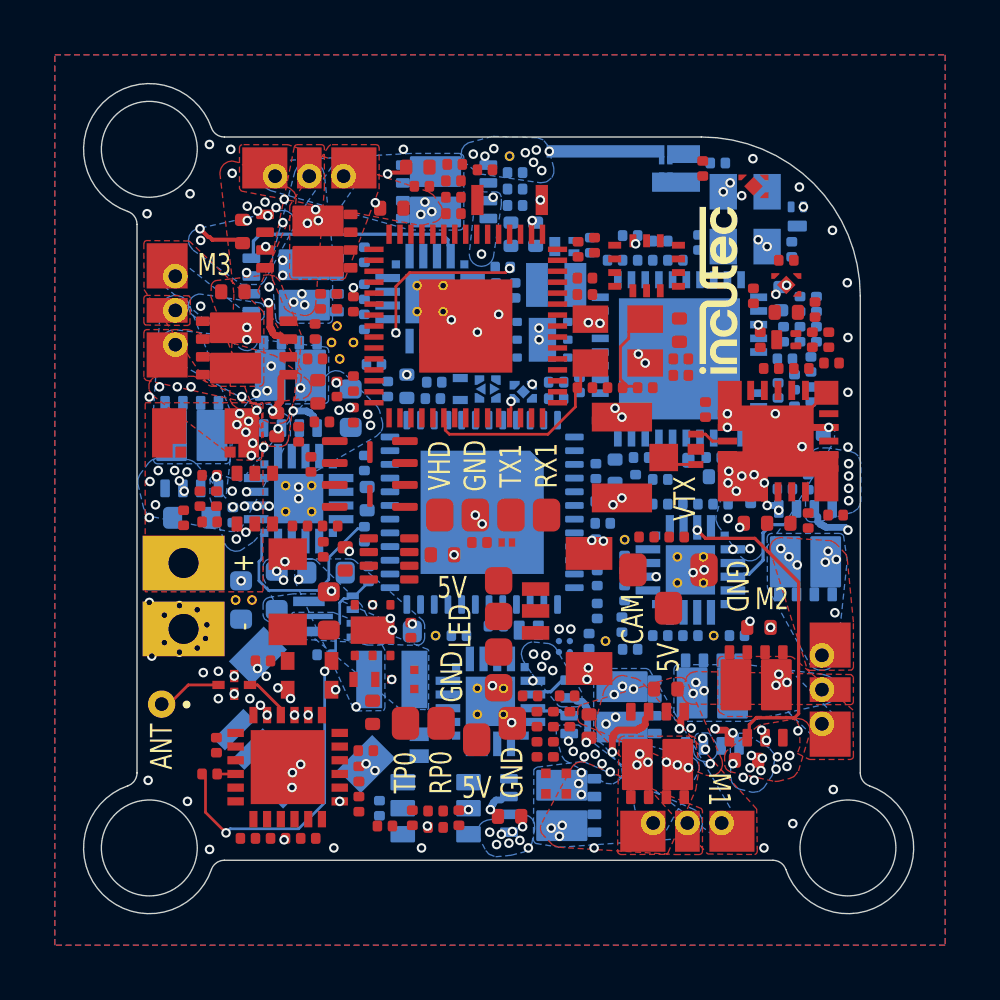
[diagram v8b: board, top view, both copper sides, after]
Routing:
- net /ESC2/C_PWM: track 0.00 -> 11.5 mm, vias 0 -> 1
- net /RX/TCXO_OUT: track 0.00 -> 11.3 mm, vias 0 -> 2
- net +BATT: track 0.00 -> 9.57 mm, vias 0 -> 58
- net /ESC4/B_COM: track 0.00 -> 7.99 mm
- net /ESC3/BEMF_B: track 0.00 -> 6.94 mm
- net /RP2350A/XIN: track 0.00 -> 6.23 mm
- net /ESC4/BEMF_B: track 0.00 -> 6.12 mm, vias 0 -> 2
- net GND: track 0.00 -> 4.34 mm, vias 0 -> 188
- net /ESC2/A_PWM: track 0.00 -> 3.31 mm
- net /POWER/U2_FB: track 0.00 -> 2.60 mm
- net /RP2350A/XOUT_X: track 0.00 -> 2.48 mm
- net /RX/RF_RX_ANT: track 0.00 -> 1.95 mm
- net /RX/RF_RFIO: track 0.00 -> 1.73 mm
- net /VTX/RF_PA_OUT: track 0.00 -> 1.26 mm
- net /VTX/RF_UFL: track 0.00 -> 1.18 mm
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- added copper zone on B.Cu, net +5V_BST
- added copper zone on B.Cu, net +BATT
- added copper zone on F.Cu, net +BATT
- added copper zone on In3.Cu, net +BATT
- added copper zone on F.Cu, net +BATT_IN
- added copper zone on B.Cu, net /ESC1/PHASE_A
- added copper zone on F.Cu, net /ESC1/PHASE_A
- added copper zone on B.Cu, net /ESC1/PHASE_B
- added copper zone on F.Cu, net /ESC1/PHASE_B
- added copper zone on B.Cu, net /ESC1/PHASE_C
- added copper zone on F.Cu, net /ESC1/PHASE_C
- added copper zone on B.Cu, net /ESC2/PHASE_A
- added copper zone on F.Cu, net /ESC2/PHASE_A
- added copper zone on B.Cu, net /ESC2/PHASE_B
- added copper zone on F.Cu, net /ESC2/PHASE_B
- added copper zone on B.Cu, net /ESC2/PHASE_C
- added copper zone on F.Cu, net /ESC2/PHASE_C
- added copper zone on B.Cu, net /ESC3/PHASE_A
- added copper zone on F.Cu, net /ESC3/PHASE_A
- added copper zone on B.Cu, net /ESC3/PHASE_B
- added copper zone on F.Cu, net /ESC3/PHASE_B
- added copper zone on B.Cu, net /ESC3/PHASE_C
- added copper zone on F.Cu, net /ESC3/PHASE_C
- added copper zone on B.Cu, net /ESC4/PHASE_A
- added copper zone on F.Cu, net /ESC4/PHASE_A
- added copper zone on B.Cu, net /ESC4/PHASE_B
- added copper zone on F.Cu, net /ESC4/PHASE_B
- added copper zone on B.Cu, net /ESC4/PHASE_C
- added copper zone on F.Cu, net /ESC4/PHASE_C
- added copper zone on B.Cu, net /POWER/U2_SW
- added copper zone on B.Cu, net GND
- added copper zone on F.Cu, net GND
- added copper zone on In1.Cu, net GND
- added copper zone on In2.Cu, net GND
- added copper zone on In4.Cu, net GND
